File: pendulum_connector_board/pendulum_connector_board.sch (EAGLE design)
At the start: 9 parts, among them X1 SM07B-SRSS-TB

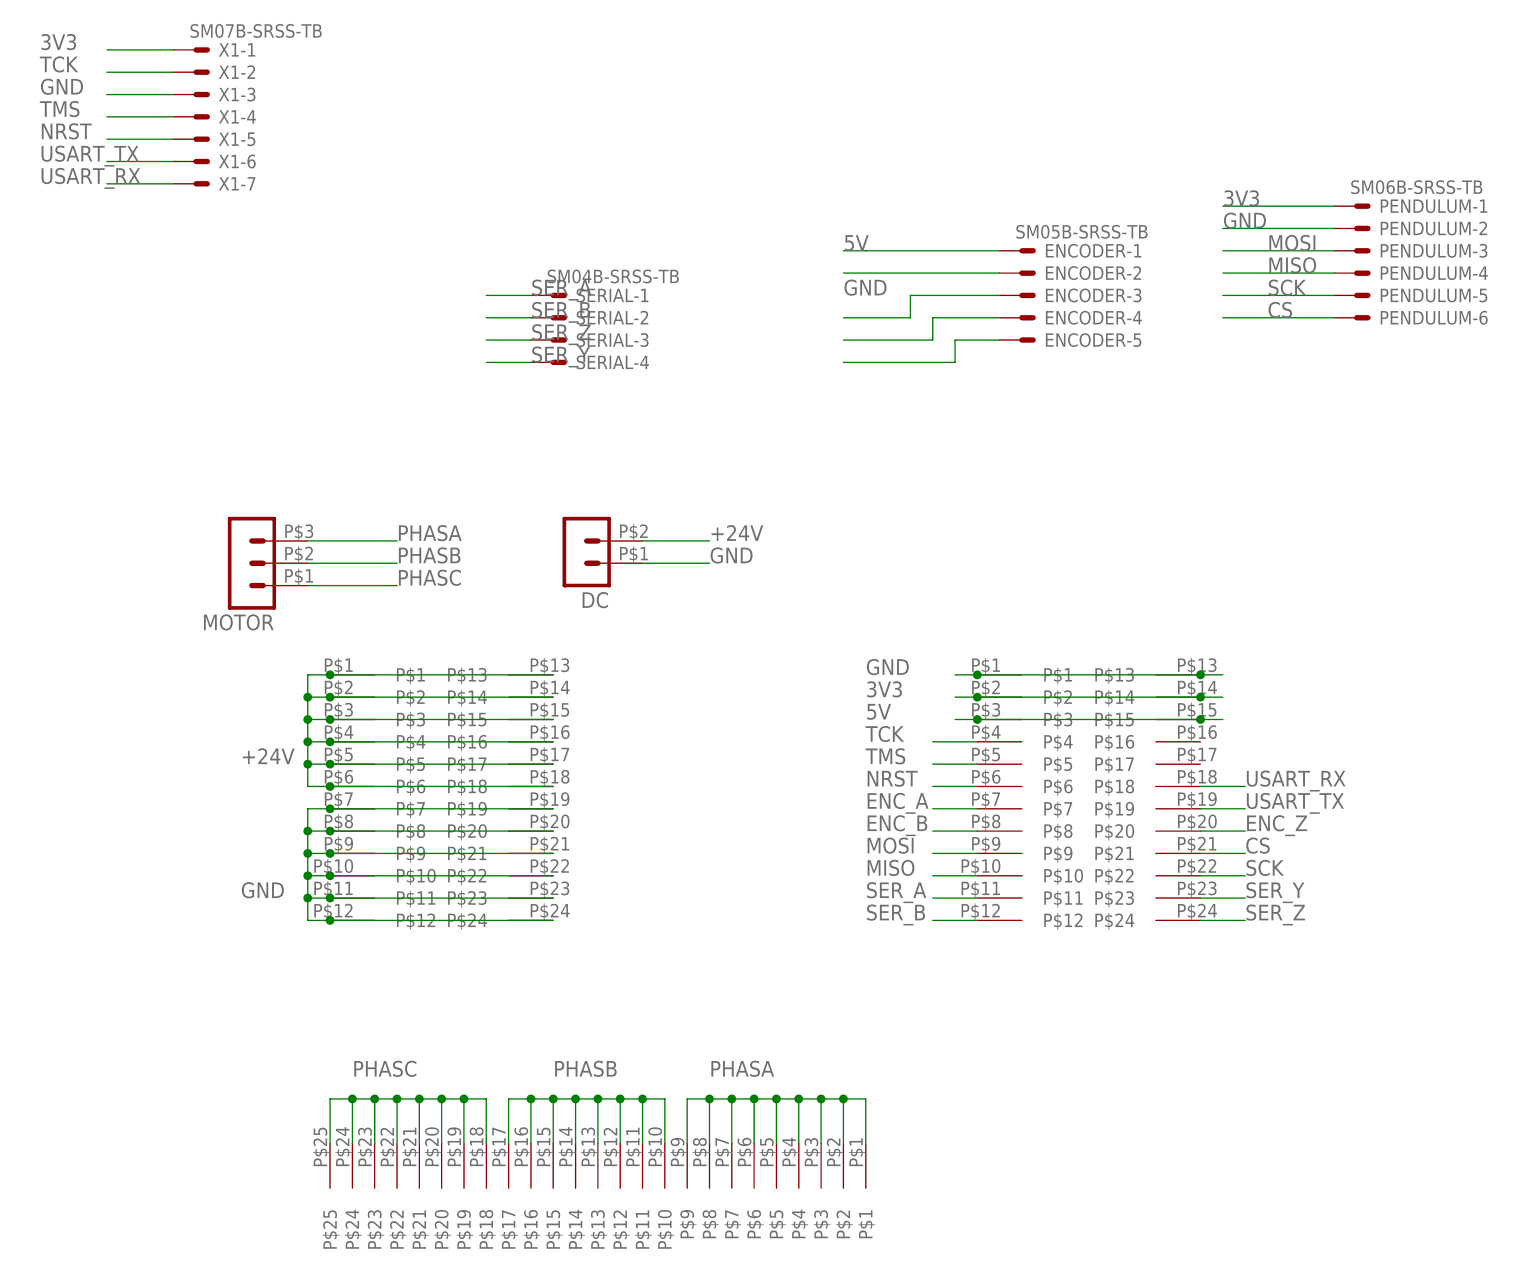
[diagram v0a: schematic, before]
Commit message: Pendulum control demo in python
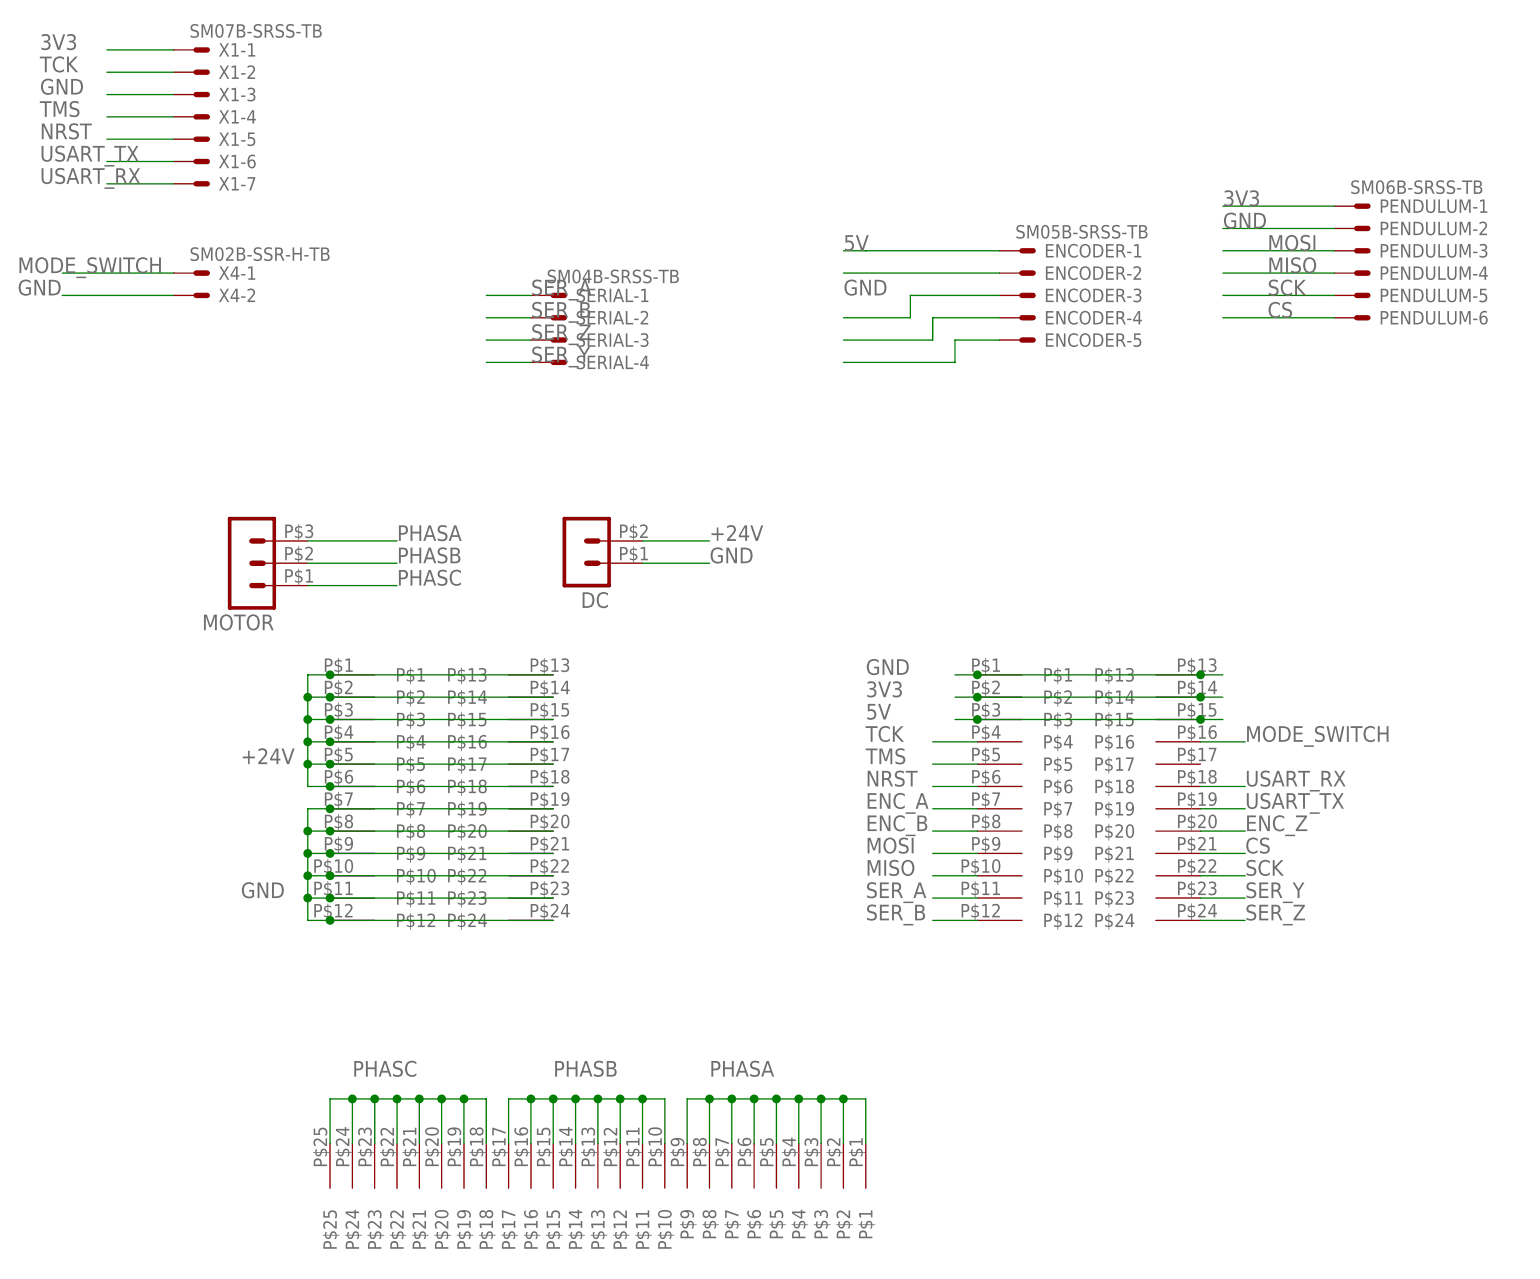
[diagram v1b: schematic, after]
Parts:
- added X4: SM02B-SSR-H-TB, con-jst2:SM02B-SSR-H-TB
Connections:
- new net MODE_SWITCH: U$2.P$16, X4-1.S
- net GND: now also X4-2.S
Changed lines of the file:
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@@
 <part name="U$2" library="Ben_Library" deviceset="HEADER_2X12" device=""/>
 <part name="X1" library="con-jst2" deviceset="?M07B-SRSS-TB" device="S" value="SM07B-SRSS-TB"/>
+<part name="X4" library="con-jst2" deviceset="SM02B-SSR-H-TB" device=""/>
 </parts>
 <sheets>
@@
 <instance part="X1" gate="-6" x="5.08" y="71.12"/>
 <instance part="X1" gate="-7" x="5.08" y="68.58"/>
+<instance part="X4" gate="-1" x="5.08" y="58.42"/>
+<instance part="X4" gate="-2" x="5.08" y="55.88"/>
 </instances>
 <busses>
@@
 <pinref part="X1" gate="-3" pin="S"/>
 </segment>
+<segment>
+<pinref part="X4" gate="-2" pin="S"/>
+<wire x1="2.54" y1="55.88" x2="-10.16" y2="55.88" width="0.1524" layer="91"/>
+<label x="-15.24" y="55.88" size="1.778" layer="95"/>
+</segment>
 </net>
 <net name="+24V" class="0">
@@
 </segment>
 </net>
+<net name="MODE_SWITCH" class="0">
+<segment>
+<pinref part="X4" gate="-1" pin="S"/>
+<wire x1="2.54" y1="58.42" x2="-10.16" y2="58.42" width="0.1524" layer="91"/>
+<label x="-15.24" y="58.42" size="1.778" layer="95"/>
+</segment>
+<segment>
+<pinref part="U$2" gate="G$1" pin="P$16"/>
+<wire x1="119.38" y1="5.08" x2="124.46" y2="5.08" width="0.1524" layer="91"/>
+<label x="124.46" y="5.08" size="1.778" layer="95"/>
+</segment>
+</net>

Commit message: updated boards
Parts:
- added C1, C2, C3: (no value), rcl:CPOL-USE2.5-6
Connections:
- net +24V: now also C1.+, C2.+, C3.+
- net GND: now also C1.-, C2.-, C3.-
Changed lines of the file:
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@@
 <part name="X1" library="con-jst2" deviceset="?M07B-SRSS-TB" device="S" value="SM07B-SRSS-TB"/>
 <part name="X4" library="con-jst2" deviceset="SM02B-SSR-H-TB" device=""/>
+<part name="C1" library="rcl" deviceset="CPOL-US" device="E2.5-6"/>
+<part name="C2" library="rcl" deviceset="CPOL-US" device="E2.5-6"/>
+<part name="C3" library="rcl" deviceset="CPOL-US" device="E2.5-6"/>
 </parts>
 <sheets>
@@
 <instance part="X4" gate="-1" x="5.08" y="58.42"/>
 <instance part="X4" gate="-2" x="5.08" y="55.88"/>
+<instance part="C1" gate="G$1" x="114.3" y="-35.56"/>
+<instance part="C2" gate="G$1" x="119.38" y="-35.56"/>
+<instance part="C3" gate="G$1" x="124.46" y="-35.56"/>
 </instances>
 <busses>
@@
 <label x="-15.24" y="55.88" size="1.778" layer="95"/>
 </segment>
+<segment>
+<wire x1="132.08" y1="-40.64" x2="124.46" y2="-40.64" width="0.1524" layer="91"/>
+<label x="99.06" y="-40.64" size="1.778" layer="95"/>
+<pinref part="C1" gate="G$1" pin="-"/>
+<wire x1="124.46" y1="-40.64" x2="119.38" y2="-40.64" width="0.1524" layer="91"/>
+<wire x1="119.38" y1="-40.64" x2="114.3" y2="-40.64" width="0.1524" layer="91"/>
+<wire x1="114.3" y1="-40.64" x2="101.6" y2="-40.64" width="0.1524" layer="91"/>
+<junction x="114.3" y="-40.64"/>
+<pinref part="C2" gate="G$1" pin="-"/>
+<junction x="119.38" y="-40.64"/>
+<pinref part="C3" gate="G$1" pin="-"/>
+<junction x="124.46" y="-40.64"/>
+</segment>
 </net>
 <net name="+24V" class="0">
@@
 <junction x="20.32" y="12.7"/>
 </segment>
+<segment>
+<wire x1="132.08" y1="-33.02" x2="124.46" y2="-33.02" width="0.1524" layer="91"/>
+<label x="99.06" y="-33.02" size="1.778" layer="95"/>
+<pinref part="C1" gate="G$1" pin="+"/>
+<wire x1="124.46" y1="-33.02" x2="119.38" y2="-33.02" width="0.1524" layer="91"/>
+<wire x1="119.38" y1="-33.02" x2="114.3" y2="-33.02" width="0.1524" layer="91"/>
+<wire x1="114.3" y1="-33.02" x2="101.6" y2="-33.02" width="0.1524" layer="91"/>
+<junction x="114.3" y="-33.02"/>
+<pinref part="C2" gate="G$1" pin="+"/>
+<junction x="119.38" y="-33.02"/>
+<pinref part="C3" gate="G$1" pin="+"/>
+<junction x="124.46" y="-33.02"/>
+</segment>
 </net>

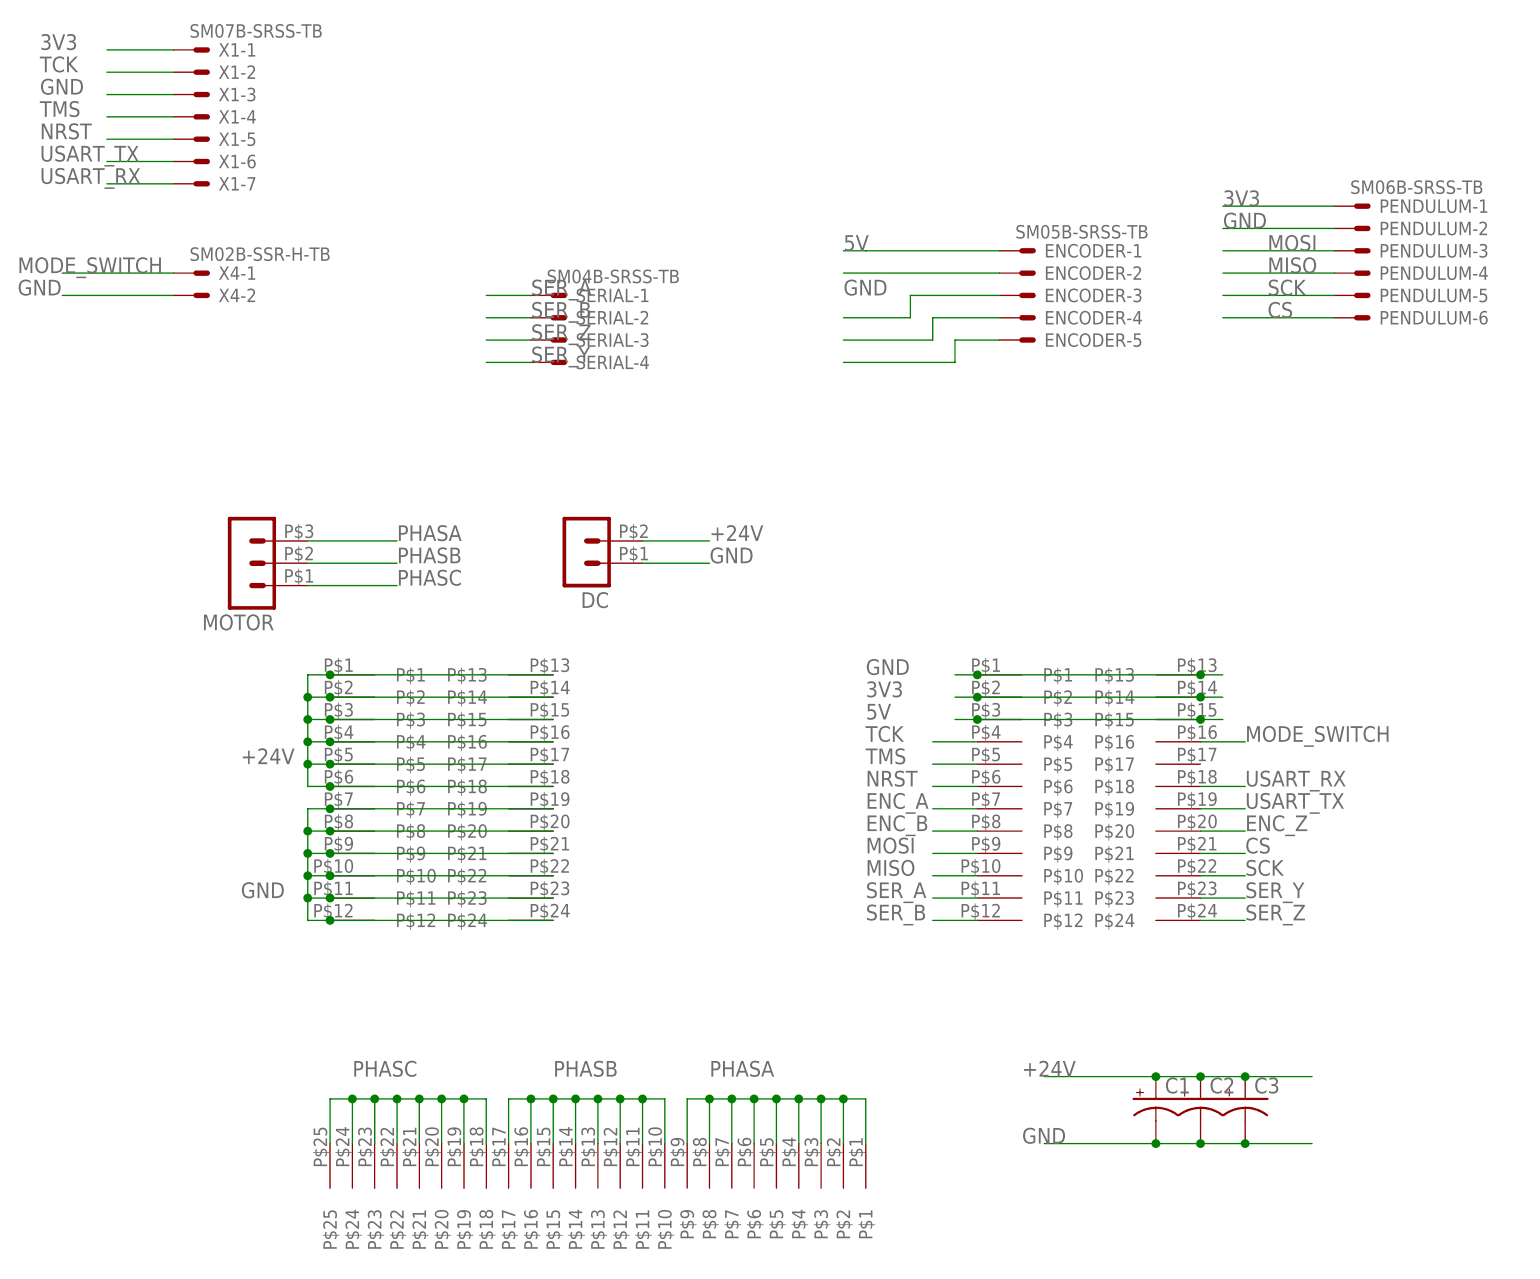
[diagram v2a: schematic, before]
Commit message: fixing controller BOM mistake
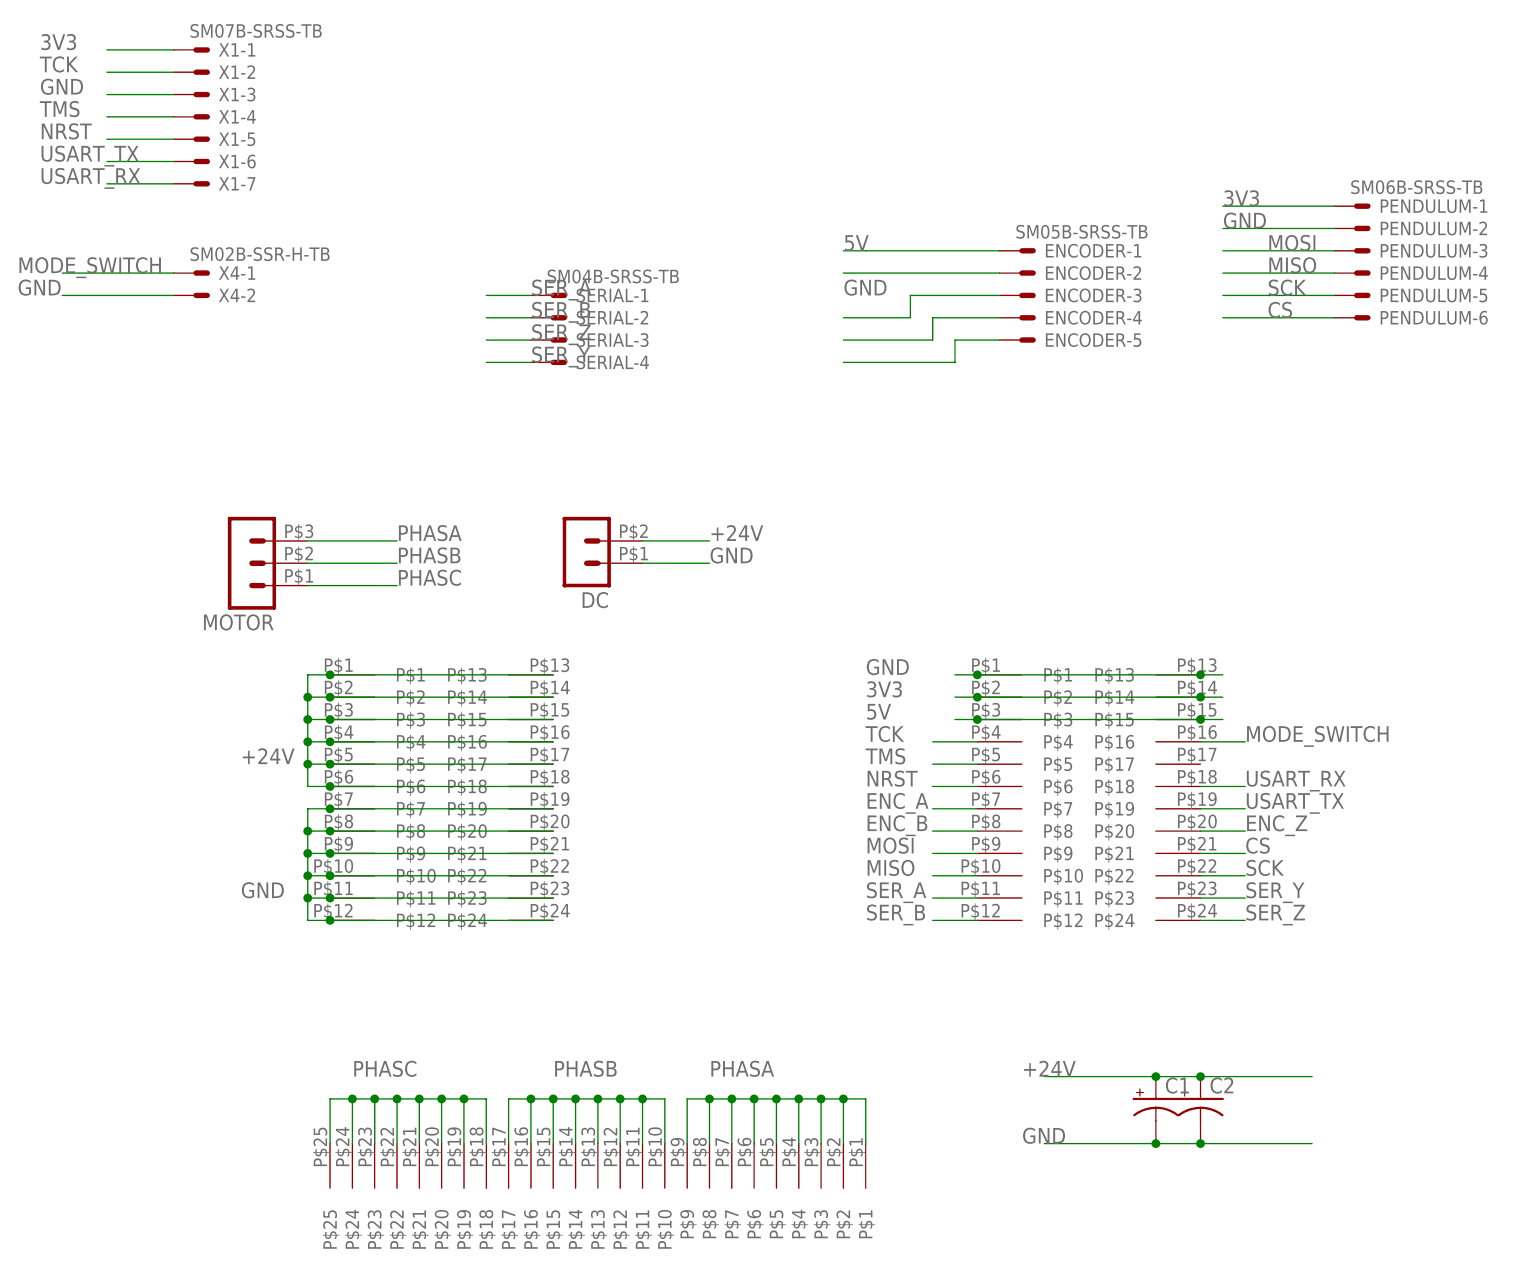
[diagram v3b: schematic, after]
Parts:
- removed C3: (no value), rcl:CPOL-USE2.5-6
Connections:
- net +24V: no longer C3.+
- net GND: no longer C3.-
